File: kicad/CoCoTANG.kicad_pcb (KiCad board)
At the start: 2 copper layers, 215.9 x 85.1 mm, 108 parts, among them J1 CPU, J10 PIA1_OUT, J13 CoCo_Cart, J14 PIA0_IN, J15 PIA1_IN, J17 AV_IN, J18 CMP_IN, J2 ADDRMUX_OUT, J20 AV_OUT, J21 CMP_OUT, J23 TRG, J28 ADDRMUX, J3 ADDRMUX_IN, J4 PIA0, J5 PIA1, J6 CLK, J7 AV_HEADER, J8 PIA0_OUT, Q1 MMBT3904-TP, Q2 MMBT3904-TP, Q3 MMBT3904-TP, Q4 MMBT3904-TP, Q5 MMBT3904-TP, Q6 MMBT3904-TP, Q7 MMBT3904-TP, Q8 MMBT3904-TP, Q9 MMBT3904-TP, U1 74HC138, U10 74LVC245, U11 74LVC245, U12 74LVC245, U2 AT28C64B-15PU, U22 74HC11, U3 74HC139, U5 Tang_Nano_20k, U7 74HC30, U8 74LVC245, U9 74HC245

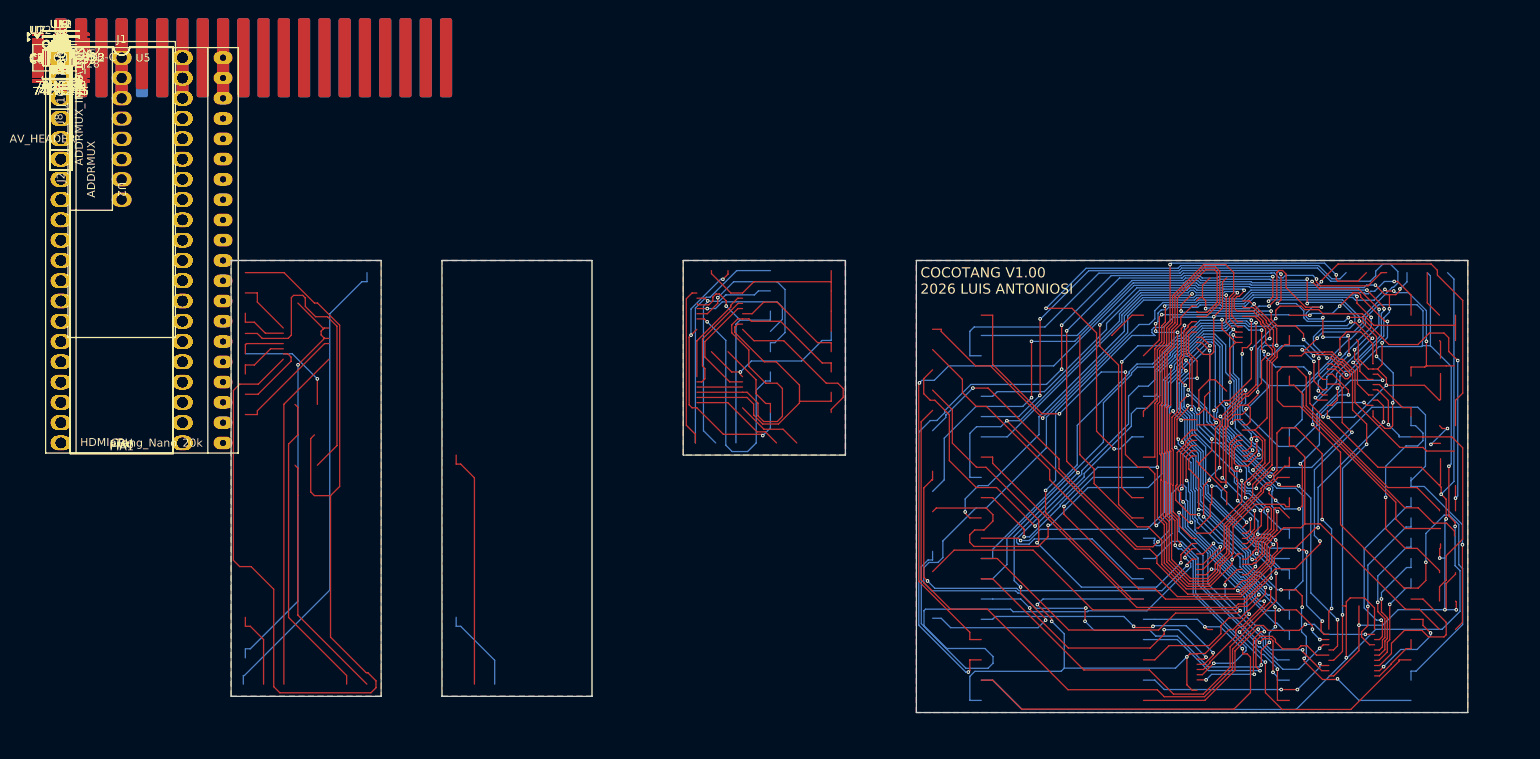
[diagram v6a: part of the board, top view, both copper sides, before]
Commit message: fix missing board pin
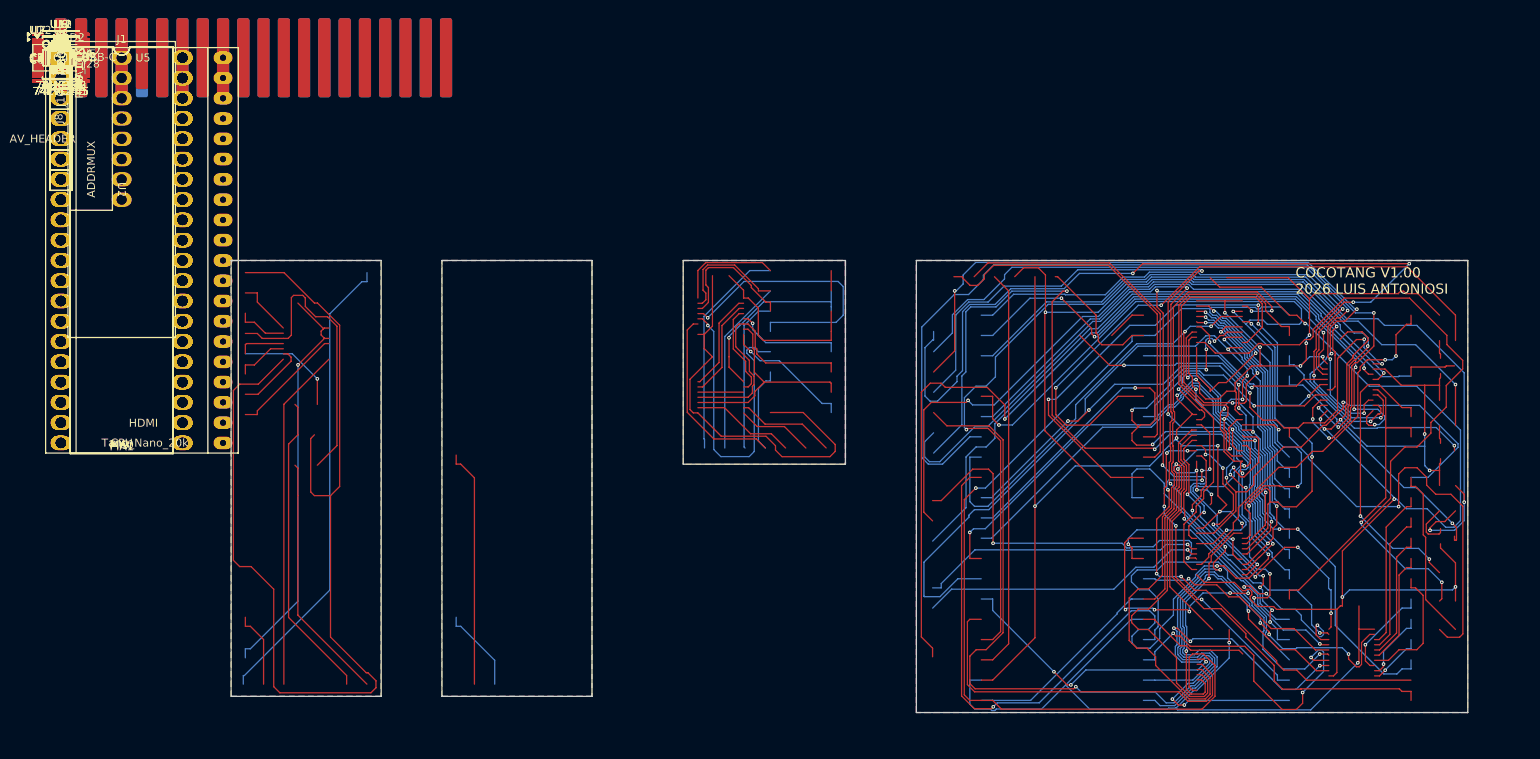
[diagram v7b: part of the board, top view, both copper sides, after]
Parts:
- J2, J3: footprint Connector_PinHeader_2.54mm:PinHeader_1x06_P2.54mm_Vertical -> Connector_PinHeader_2.54mm:PinHeader_1x07_P2.54mm_Vertical
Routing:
- net GND: track 897.6 -> 1016.9 mm, vias 24 -> 15
- net ~{HALT}: track 155.7 -> 46.9 mm, vias 8 -> 2
- net R/~{W}: track 70.4 -> 168.3 mm
- net D3_33: track 115.2 -> 27.1 mm, vias 5 -> 1
- net D5_33: track 107.8 -> 40.0 mm, vias 8 -> 3
- net ~{HS_33}: track 120.5 -> 60.0 mm, vias 10 -> 1
- net CVBS_33: track 136.7 -> 79.8 mm, vias 4 -> 0
- net Net-(Q8-Pad1): track 62.1 -> 5.82 mm
- net MP3_33: track 134.2 -> 81.9 mm, vias 6 -> 8
- net A14: track 108.2 -> 63.2 mm, vias 7 -> 6
- net ~{SLENB}: track 83.0 -> 127.8 mm
- net A1: track 99.0 -> 54.3 mm, vias 0 -> 1
- net A2: track 100.9 -> 56.4 mm, vias 0 -> 1
- net A7: track 71.8 -> 113.0 mm, vias 1 -> 0
- net D0_33: track 79.3 -> 40.2 mm, vias 6 -> 1
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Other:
- outline, holes or cut-outs redrawn

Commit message: final board/gerber files
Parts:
- removed C13, C14, C16: 470pF, Capacitor_SMD:C_0805_2012Metric_Pad1.18x1.45mm_HandSolder
- removed C15: 1uF, Capacitor_SMD:C_0805_2012Metric_Pad1.18x1.45mm_HandSolder
- removed C22: 6.8nF, Capacitor_SMD:C_0805_2012Metric_Pad1.18x1.45mm_HandSolder
- removed C23: 4.7uF, Capacitor_SMD:C_0805_2012Metric_Pad1.18x1.45mm_HandSolder
- removed C26, C27, C28: 104, Capacitor_SMD:C_0805_2012Metric_Pad1.18x1.45mm_HandSolder
- removed J10: PIA1_OUT, Connector_PinHeader_2.54mm:PinHeader_1x02_P2.54mm_Vertical
- removed J17: AV_IN, Connector_PinHeader_2.54mm:PinHeader_1x06_P2.54mm_Vertical
- removed J20: AV_OUT, Connector_PinHeader_2.54mm:PinHeader_1x05_P2.54mm_Vertical
- removed J5: PIA1, FPGA_Common:DIP-40_W15.24mm-OVERSIZED
- removed Q1, Q3, Q6: MMBT3904-TP, FPGA_Common:SOT-23_MCC
- removed R13, R14, R15: 75, Resistor_SMD:R_0805_2012Metric_Pad1.20x1.40mm_HandSolder
- removed R18, R25, R27, R29, R37, R38, R39: 1K, Resistor_SMD:R_0805_2012Metric_Pad1.20x1.40mm_HandSolder
- removed R22: 100K, Resistor_SMD:R_0805_2012Metric_Pad1.20x1.40mm_HandSolder
- removed R26, R28, R30: 4.7K, Resistor_SMD:R_0805_2012Metric_Pad1.20x1.40mm_HandSolder
- added C17: 1uF, Capacitor_SMD:C_0805_2012Metric_Pad1.18x1.45mm_HandSolder, F.Cu at (0.00, 0.00)
- added JP2: RGB, Jumper:SolderJumper-2_P1.3mm_Open_Pad1.0x1.5mm, F.Cu at (0.00, 0.00)
- added JP3: PIA0, Jumper:SolderJumper-2_P1.3mm_Open_Pad1.0x1.5mm, F.Cu at (0.00, 0.00)
- added JP4: PIA1, Jumper:SolderJumper-2_P1.3mm_Open_Pad1.0x1.5mm, F.Cu at (0.00, 0.00)
- added RN1, RN2: R_Network08, Resistor_THT:R_Array_SIP9, F.Cu at (0.00, 0.00)
- C1, C2, C3, C32, C33, C4, C5, C6, C7: moved to B.Cu
- JP1: value Jumper_2_Open -> AUTOSTART
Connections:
- net PR_RCA renamed R_CVBS
- net Y_33 renamed G_Y_33
- net Y_RCA renamed G_Y
- C9 pad 1: PB_RCA -> B_CHR
- J14 pad 1: KEYINT -> ~{FS}
- J14 pad 3: ~{FS} -> KEYINT
- J15 pad 1: SERNT -> ~{CART}
- J15 pad 2: ~{CART} -> SERNT
- J18 pad 2: PB_33 -> B_CHR_33
- J18 pad 3: PR_33 -> R_CVBS_33
- J21 pad 2: PB_RCA -> B_CHR
- J4 pad 10: AP10 -> PB10/SERNT
- J4 pad 18: ~{FS} -> ~{FS/CART}
- J7 pad 2: CHR_33 -> B_CHR_33
- J7 pad 3: CVBS_33 -> R_CVBS_33
- J8 pad 1: ~{HS} -> ~{FS/CART}
- J8 pad 2: ~{FS} -> ~{HS}/SERNT
- R11 pad 2: PB_RCA -> Net-(JP2-A)
- R33 pad 1: PB_33 -> B_CHR_33
- R35 pad 1: PR_33 -> R_CVBS_33
- U5 pad 18: CVBS_33 -> R_CVBS_33
- U5 pad 33: CHR_33 -> B_CHR_33
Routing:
- net GND: track 1016.9 -> 620.4 mm, vias 15 -> 14
- net +3.3V: track 407.2 -> 293.1 mm, vias 15 -> 11
- net CVBS_33: track 79.8 -> 0.00 mm
- net R_CVBS_33: track 0.00 -> 75.9 mm
- net MP2_33: track 159.0 -> 83.8 mm, vias 9 -> 2
- net ~{SLENB}: track 127.8 -> 61.9 mm, vias 3 -> 2
- net AUDIO_33: track 155.6 -> 93.2 mm, vias 5 -> 3
- net S0: track 157.8 -> 98.7 mm, vias 5 -> 2
- net S2_33: track 113.6 -> 54.8 mm, vias 3 -> 1
- net B_CHR_33: track 0.00 -> 46.7 mm
- net CHR_33: track 46.3 -> 0.00 mm
- net G_Y: track 71.5 -> 28.2 mm
- net ~{RESET}: track 83.0 -> 41.9 mm, vias 3 -> 2
- net ~{NMI}: track 55.2 -> 14.3 mm, vias 0 -> 1
- net ~{DATAEN}: track 138.3 -> 98.4 mm, vias 4 -> 2
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- added copper zone on B.Cu, net A11
- added copper zone on F.Cu, net A11
- removed copper zone on B.Cu, net GND
- removed copper zone on F.Cu, net GND
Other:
- board size 215.9 x 85.1 mm -> 187.5 x 58.4 mm
- board text added: "B/CHR"
- board text added: "G/Y"
- board text added: "PIA0"
- board text added: "R/CVBS"
- board text removed: "CHR"
- board text removed: "CVBS"
- board text removed: "CVBS VIDEO 1.1"
- board text removed: "PB/B"
- board text removed: "PR/R"
- board text removed: "Y"
- board text removed: "Y/G"
